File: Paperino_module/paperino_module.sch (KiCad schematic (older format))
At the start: 23 parts, among them P1 CONN_01X06, P2 CONN_01X06, P3 CONN_01X06, P4 CONN_01X06, Q1 PMOS, Q2 NMOS, U1 BMA250E, X1 XF2M-2615-1A, X2 XF2B-4545-1A

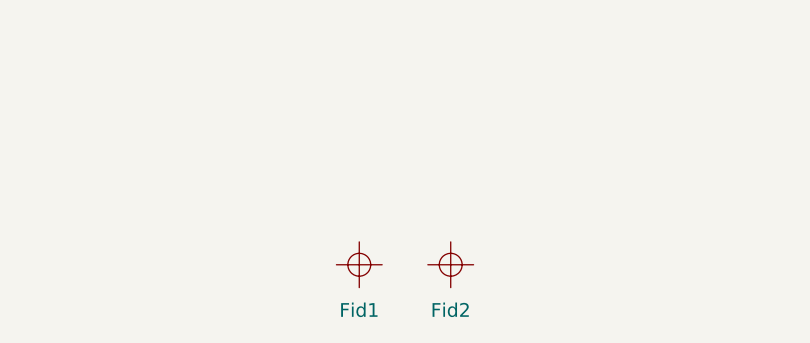
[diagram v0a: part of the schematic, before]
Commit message: renaming and deleting fids
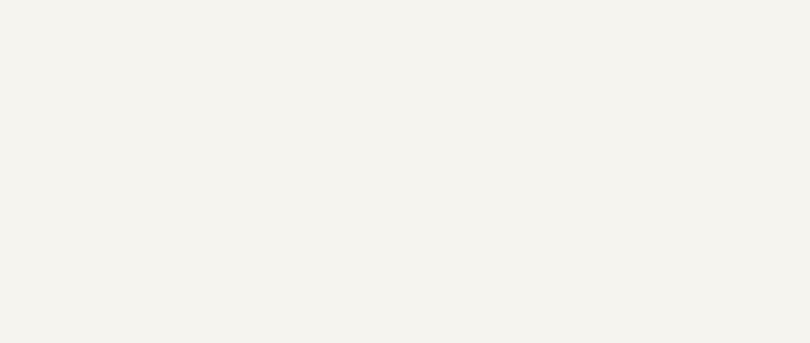
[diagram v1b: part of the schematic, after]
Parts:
- removed Fid1, Fid2: Fiducial, Paperino:Fiducial, symbol Fiducial
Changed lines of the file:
@@
 LIBS:valves
 LIBS:paperino
-LIBS:paperino-cache
 EELAYER 25 0
 EELAYER END
@@
 	6500 3850 6500 4300
 Connection ~ 6500 3950
-$Comp
-L Fiducial Fid1
-U 1 1 58B53A2F
-P 6300 7450
-F 0 "Fid1" H 6300 7250 60  0000 C CNN
-F 1 "Fiducial" H 6300 7700 60  0001 C CNN
-F 2 "Paperino:Fiducial" H 6300 7450 60  0001 C CNN
-F 3 "" H 6300 7450 60  0001 C CNN
-F 4 "N/A" H 6300 7450 60  0001 C CNN "MFG Name"
-F 5 "N/A" H 6300 7450 60  0001 C CNN "MFG Part Num"
-	1    6300 7450
-	1    0    0    -1
-$EndComp
-$Comp
-L Fiducial Fid2
-U 1 1 58B53F28
-P 6700 7450
-F 0 "Fid2" H 6700 7250 60  0000 C CNN
-F 1 "Fiducial" H 6700 7700 60  0001 C CNN
-F 2 "Paperino:Fiducial" H 6700 7450 60  0001 C CNN
-F 3 "" H 6700 7450 60  0001 C CNN
-F 4 "N/A" H 6700 7450 60  0001 C CNN "MFG Name"
-F 5 "N/A" H 6700 7450 60  0001 C CNN "MFG Part Num"
-	1    6700 7450
-	1    0    0    -1
-$EndComp
 $EndSCHEMATC

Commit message: component change
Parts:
- D1, D2: footprint Diodes_SMD:D_SOD-323 -> Paperino:SOD-523F; MFG Name ON Semiconductor -> Fairchild Semiconductor; MFG Part Num RB751V40T1G -> RB751S40
- Q1: footprint Paperino:SC-59 -> Paperino:SOT-23; MFG Name Infineon Technologies -> Diodes Inc.; MFG Part Num BSR315PH6327XTSA1 -> DMP3099L-7
- Q2: footprint TO_SOT_Packages_SMD:SOT-323_SC-70 -> Paperino:SOT-23; MFG Name Vishay Siliconix -> Infineon; MFG Part Num SI1308EDL-T1-GE3 -> BSS670S2LH6327XTSA1
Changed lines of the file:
@@
 LIBS:valves
 LIBS:paperino
+LIBS:paperino_module-cache
 EELAYER 25 0
 EELAYER END
@@
 F 0 "Q2" H 6600 5300 50  0000 L CNN
 F 1 "NMOS" H 6600 5250 50  0001 L CNN
-F 2 "TO_SOT_Packages_SMD:SOT-323_SC-70" H 6600 5400 50  0001 C CNN
+F 2 "Paperino:SOT-23" H 6600 5400 50  0001 C CNN
 F 3 "" H 6400 5300 50  0000 C CNN
-F 4 "Vishay Siliconix" H 6400 5300 60  0001 C CNN "MFG Name"
-F 5 "SI1308EDL-T1-GE3" H 6400 5300 60  0001 C CNN "MFG Part Num"
+F 4 "Infineon" H 6400 5300 60  0001 C CNN "MFG Name"
+F 5 "BSS670S2LH6327XTSA1" H 6400 5300 60  0001 C CNN "MFG Part Num"
 	1    6400 5300
 	1    0    0    -1
@@
 F 0 "Q1" H 6600 3650 50  0000 L CNN
 F 1 "PMOS" H 6600 3600 50  0001 L CNN
-F 2 "Paperino:SC-59" H 6600 3750 50  0001 C CNN
+F 2 "Paperino:SOT-23" H 6600 3750 50  0001 C CNN
 F 3 "" H 6400 3650 50  0000 C CNN
-F 4 "Infineon Technologies" H 6400 3650 60  0001 C CNN "MFG Name"
-F 5 "BSR315PH6327XTSA1" H 6400 3650 60  0001 C CNN "MFG Part Num"
+F 4 "Diodes Inc." H 6400 3650 60  0001 C CNN "MFG Name"
+F 5 "DMP3099L-7" H 6400 3650 60  0001 C CNN "MFG Part Num"
 	1    6400 3650
 	1    0    0    1
@@
 F 0 "D1" H 5950 3850 50  0000 C CNN
 F 1 "30V" H 5950 4050 50  0001 C CNN
-F 2 "Diodes_SMD:D_SOD-323" H 5950 3950 50  0001 C CNN
+F 2 "Paperino:SOD-523F" H 5950 3950 50  0001 C CNN
 F 3 "" H 5950 3950 50  0000 C CNN
-F 4 "ON Semiconductor" H 5950 3950 60  0001 C CNN "MFG Name"
-F 5 "RB751V40T1G" H 5950 3950 60  0001 C CNN "MFG Part Num"
+F 4 "Fairchild Semiconductor" H 5950 3950 60  0001 C CNN "MFG Name"
+F 5 "RB751S40" H 5950 3950 60  0001 C CNN "MFG Part Num"
 	1    5950 3950
 	-1   0    0    1
@@
 F 0 "D2" H 5950 5050 50  0000 C CNN
 F 1 "30V" H 5950 4850 50  0001 C CNN
-F 2 "Diodes_SMD:D_SOD-323" H 5950 4950 50  0001 C CNN
+F 2 "Paperino:SOD-523F" H 5950 4950 50  0001 C CNN
 F 3 "" H 5950 4950 50  0000 C CNN
-F 4 "ON Semiconductor" H 5950 4950 60  0001 C CNN "MFG Name"
-F 5 "RB751V40T1G" H 5950 4950 60  0001 C CNN "MFG Part Num"
+F 4 "Fairchild Semiconductor" H 5950 4950 60  0001 C CNN "MFG Name"
+F 5 "RB751S40" H 5950 4950 60  0001 C CNN "MFG Part Num"
 	1    5950 4950
 	1    0    0    -1

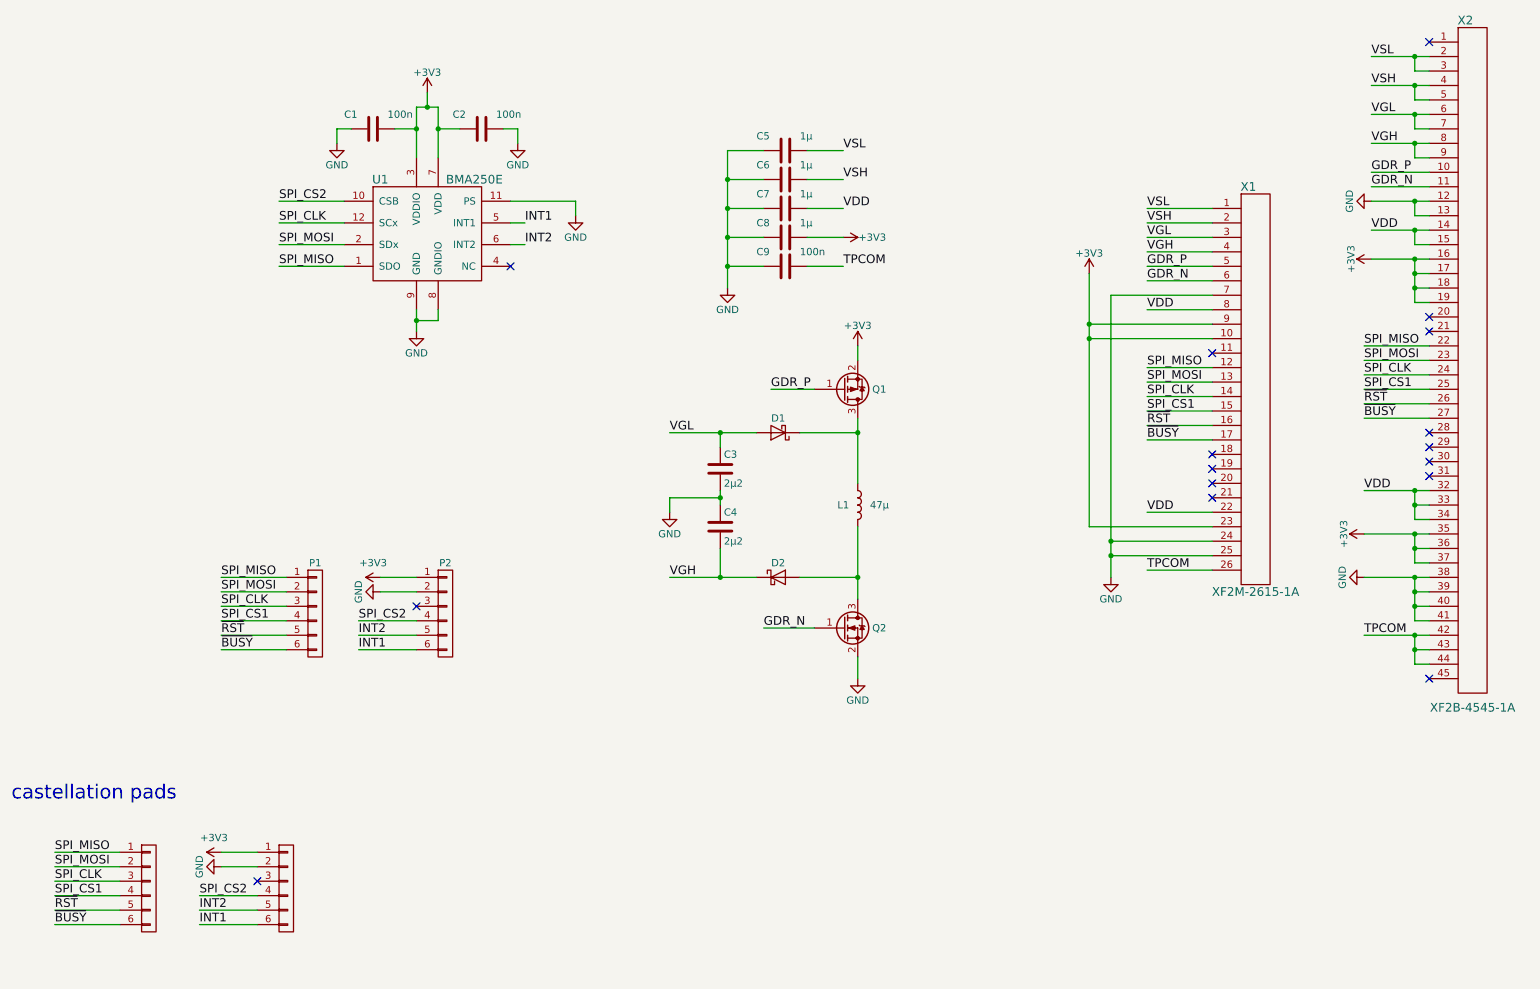
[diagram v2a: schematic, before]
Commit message: flipped connector on module
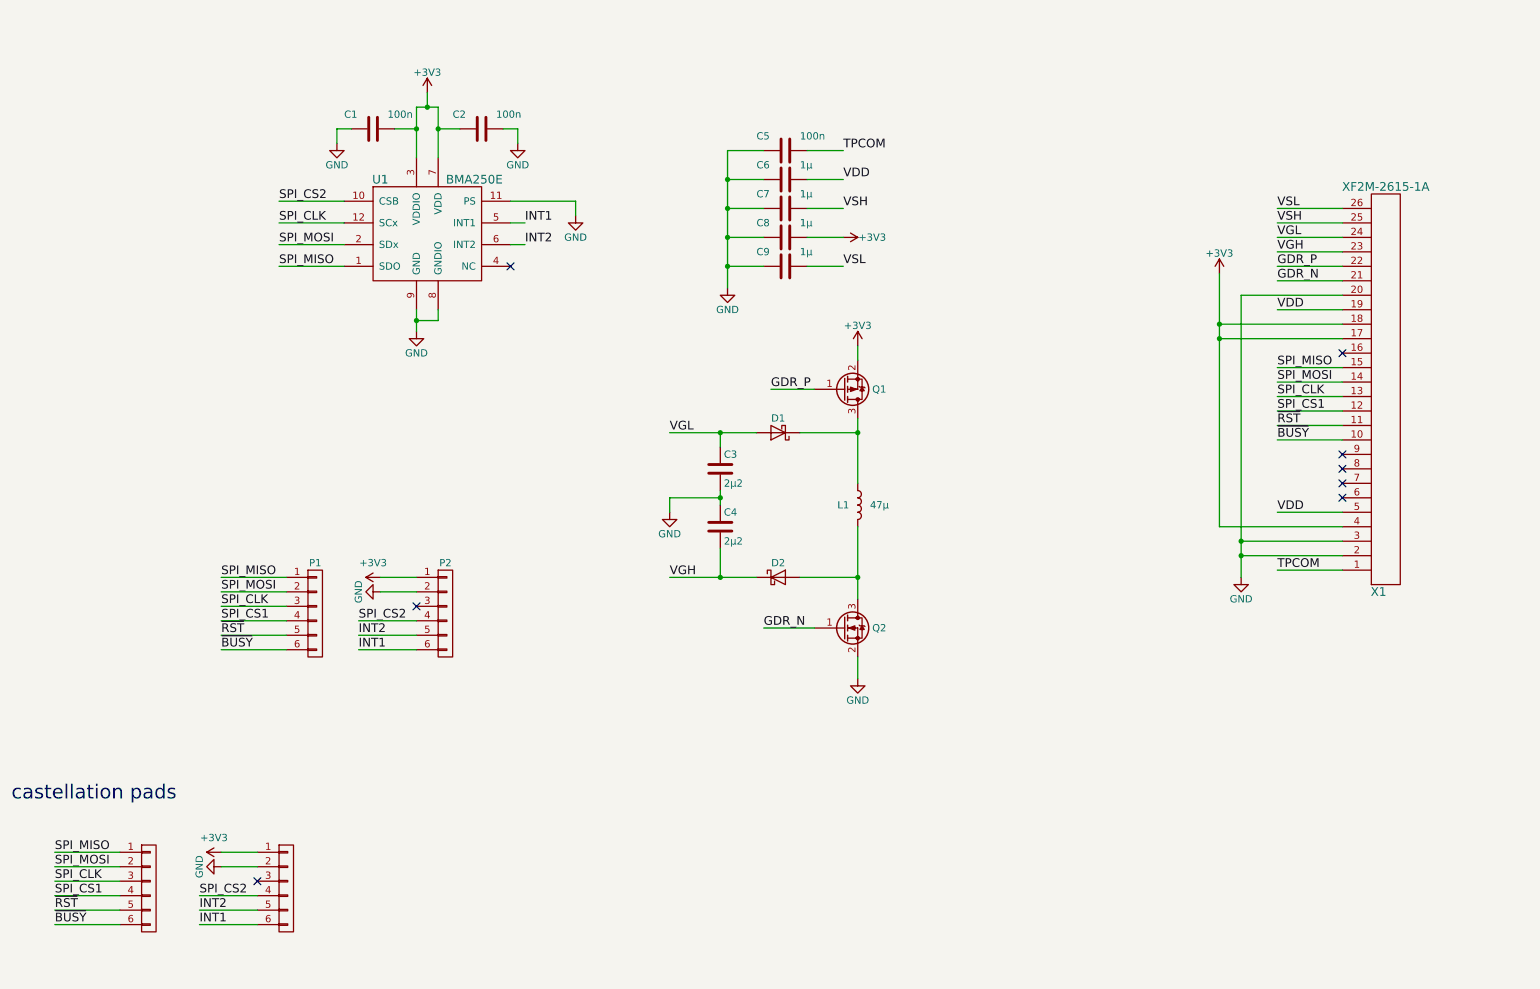
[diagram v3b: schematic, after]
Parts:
- removed X2: XF2B-4545-1A, Paperino:XF2B-4545-31A, symbol XF2B-4545-1A
- C5: value 1µ -> 100n
- C9: value 100n -> 1µ
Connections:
- net +3V3: now also X1.17, X1.18, X1.4; no longer X1.10, X1.23, X1.9
- net GDR_N: now also X1.21; no longer X1.6
- net GDR_P: now also X1.22; no longer X1.5
- net GND: now also X1.2, X1.20, X1.3; no longer X1.24, X1.25, X1.7
- net SPI_CLK: now also X1.13; no longer X1.14
- net SPI_CS1: now also X1.12; no longer X1.15
- net SPI_MISO: now also X1.15; no longer X1.12
- net SPI_MOSI: now also X1.14; no longer X1.13
- net TPCOM: now also C5.1, X1.1; no longer C9.1, X1.26
- net VDD: now also C6.1, X1.19, X1.5; no longer C7.1, X1.22, X1.8
- net VGH: now also X1.23; no longer X1.4
- net VGL: now also X1.24; no longer X1.3
- net VSH: now also C7.1, X1.25; no longer C6.1, X1.2
- net VSL: now also C9.1, X1.26; no longer C5.1, X1.1
- net ~BUSY: now also X1.10; no longer X1.17
- net ~RST: now also X1.11; no longer X1.16
- no-connect marks 16 -> 8
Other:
- moved on the sheet: X1
